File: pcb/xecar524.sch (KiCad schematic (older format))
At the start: 32 parts, among them J1 JTAG, J3 Conn_02x02_Odd_Even, U1 MCP1703A-3302_SOT89, U2 Atari_XE_Cartridge_Connector, U3 XC95144XL-TQ100, U4 SST39VF040

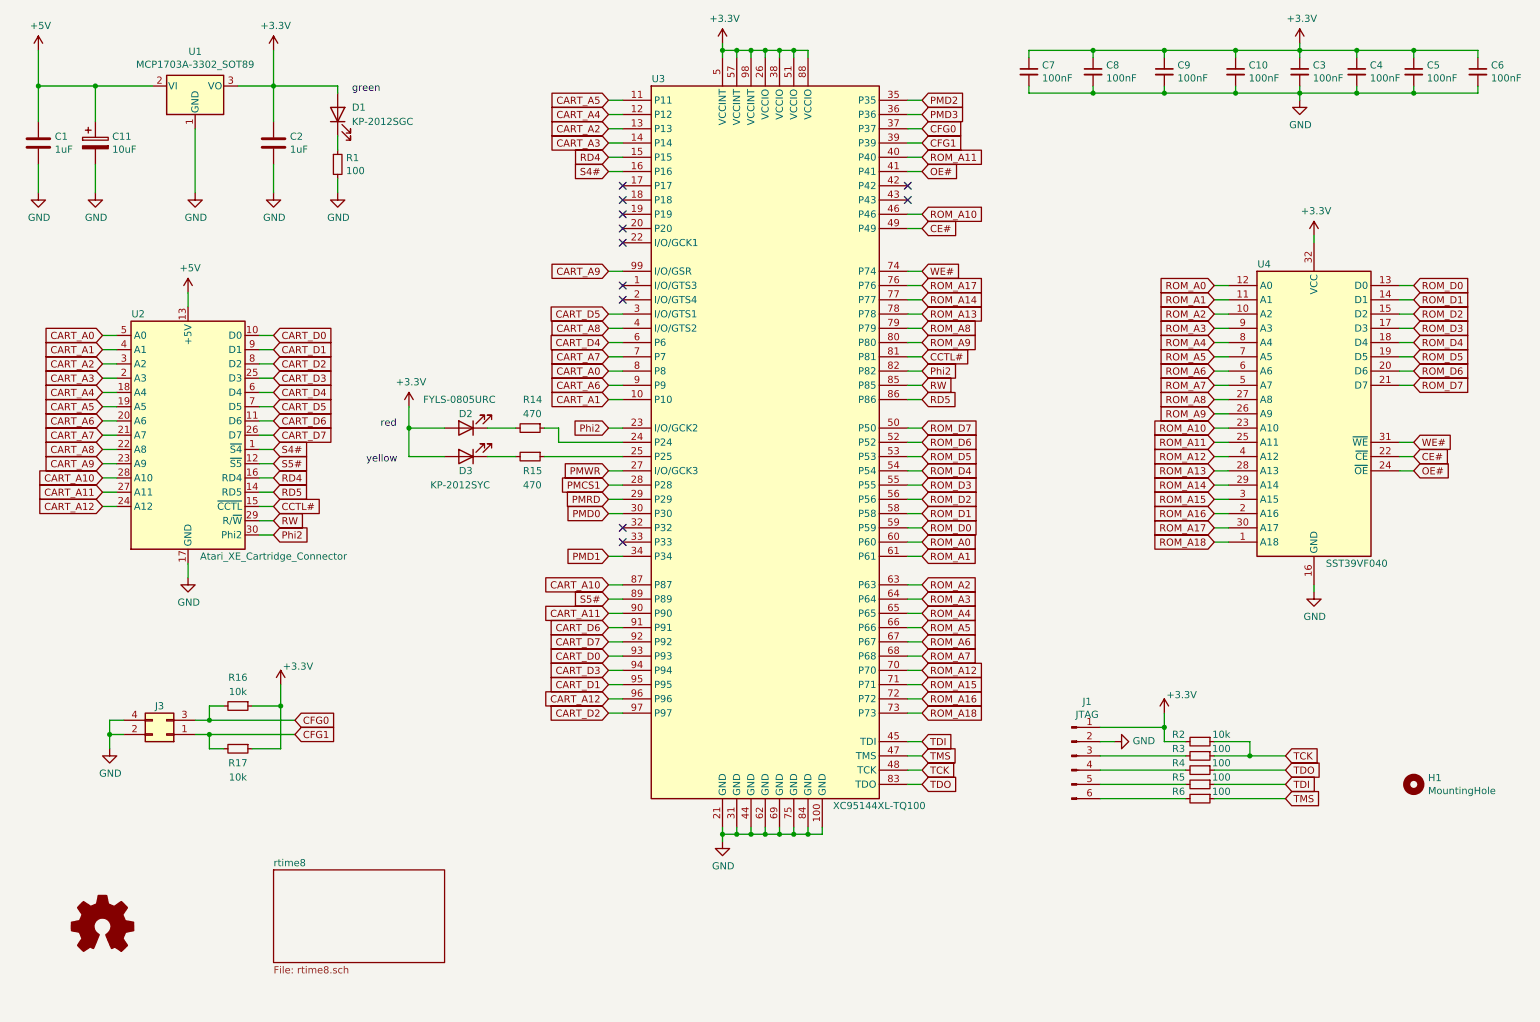
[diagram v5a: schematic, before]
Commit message: PCB, PLD: Add one configuration jumper
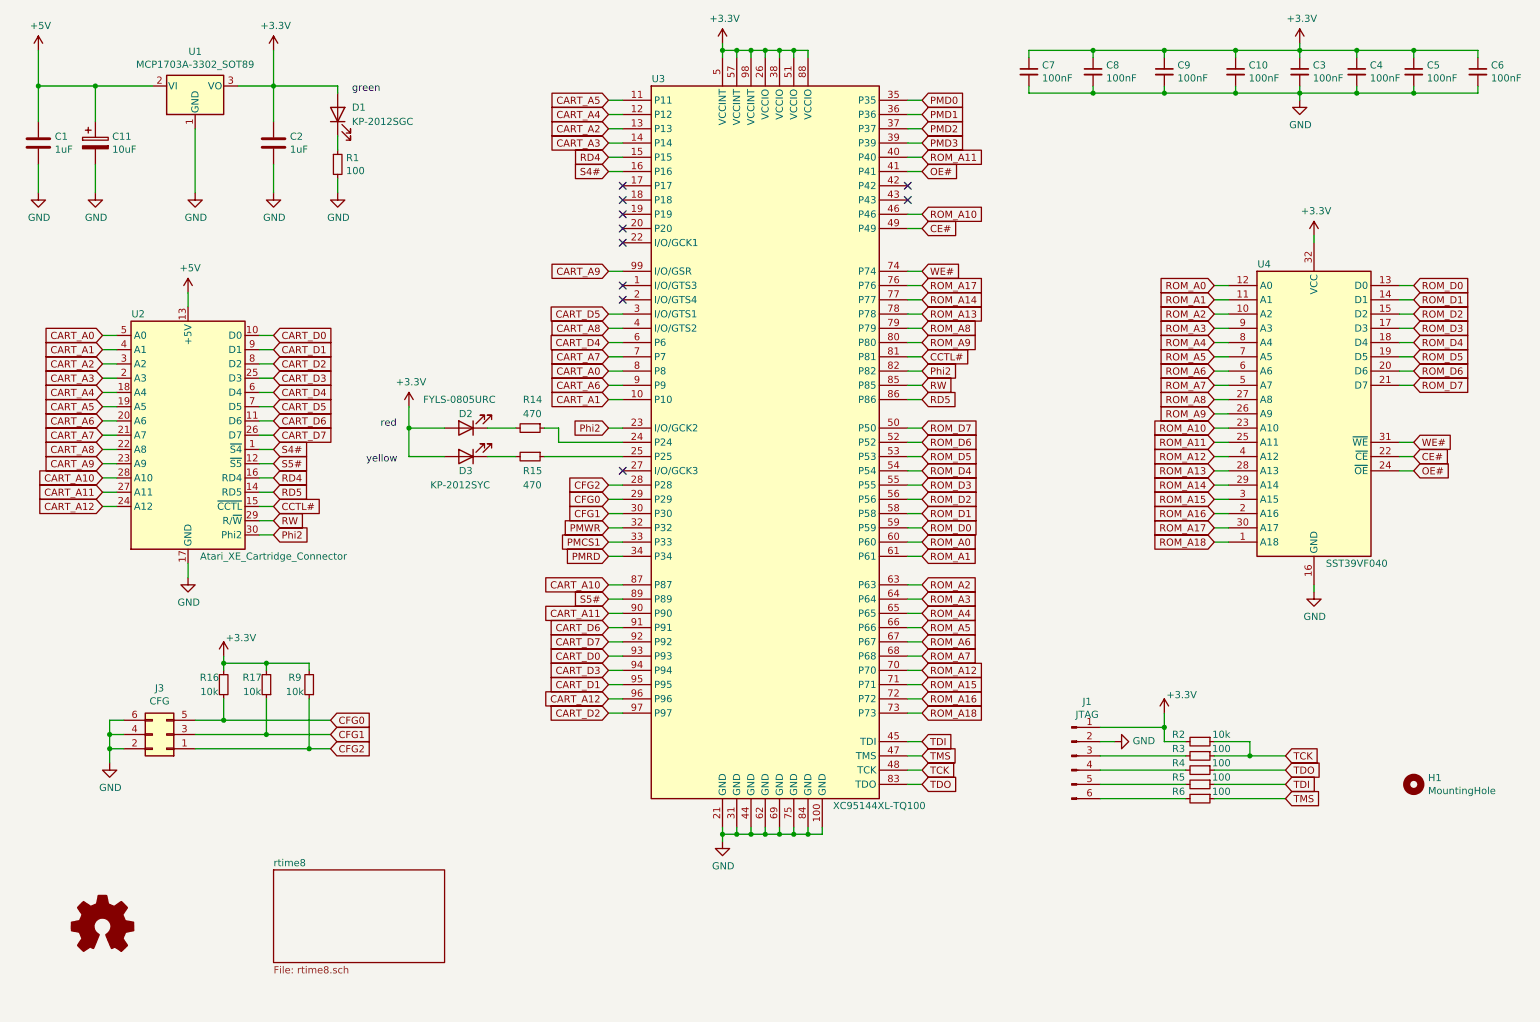
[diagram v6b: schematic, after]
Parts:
- removed J3: Conn_02x02_Odd_Even, Connector_PinHeader_2.54mm:PinHeader_2x02_P2.54mm_Horizontal, symbol Connector_Generic:Conn_02x02_Odd_Even
- added J3: CFG, Connector_PinHeader_2.54mm:PinHeader_2x03_P2.54mm_Horizontal, symbol Connector_Generic:Conn_02x03_Odd_Even
- added R9: 10k, Resistor_SMD:R_0805_2012Metric_Pad1.20x1.40mm_HandSolder, symbol Device:R_Small
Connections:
- net +3V3: now also R17.2, R9.2; no longer R17.1
- net CFG0: now also U3.29 (P29), J3.5 (Pin_5); no longer U3.37 (P37)
- net CFG1: now also R17.1, U3.30 (P30), J3.3 (Pin_3); no longer R17.2, U3.39 (P39)
- net GND: now also J3.2 (Pin_2), J3.4 (Pin_4), J3.6 (Pin_6)
- net PMCS1: now also U3.33 (P33); no longer U3.28 (P28)
- net PMD0: now also U3.35 (P35); no longer U3.30 (P30)
- net PMD1: now also U3.36 (P36); no longer U3.34 (P34)
- net PMD2: now also U3.37 (P37); no longer U3.35 (P35)
- net PMD3: now also U3.39 (P39); no longer U3.36 (P36)
- net PMRD: now also U3.34 (P34); no longer U3.29 (P29)
- net PMWR: now also U3.32 (P32); no longer U3.27 (I/O/GCK3)
- new net CFG2: J3.1 (Pin_1), R9.1, U3.28 (P28)
- no-connect marks 11 -> 10
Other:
- moved on the sheet: R16, R17
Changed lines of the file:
@@
 Text GLabel 6900 4050 2    50   Input ~ 0
 ROM_D2
-Text GLabel 4700 3950 0    50   Input ~ 0
+Text GLabel 4700 4350 0    50   Input ~ 0
 PMCS1
-Text GLabel 4700 4050 0    50   Input ~ 0
+Text GLabel 4700 4450 0    50   Input ~ 0
 PMRD
-Text GLabel 6900 1250 2    50   Input ~ 0
+Text GLabel 6900 1450 2    50   Input ~ 0
 PMD2
-Text GLabel 4700 4450 0    50   Input ~ 0
+Text GLabel 6900 1350 2    50   Input ~ 0
 PMD1
 Wire Wire Line
@@
 	4700 3950 4800 3950
 Wire Wire Line
-	4800 3850 4700 3850
+	4800 4250 4700 4250
 $Comp
 L Device:C_Polarized C11
@@
 Wire Wire Line
 	6900 1650 6800 1650
-Text GLabel 6900 1350 2    50   Input ~ 0
+Text GLabel 6900 1550 2    50   Input ~ 0
 PMD3
-Text GLabel 4700 4150 0    50   Input ~ 0
+Text GLabel 6900 1250 2    50   Input ~ 0
 PMD0
 Wire Wire Line
@@
 Wire Wire Line
 	4700 3550 4800 3550
-NoConn ~ 4800 4250
-NoConn ~ 4800 4350
+NoConn ~ 4800 3850
 NoConn ~ 4800 2650
 NoConn ~ 6800 1950
@@
 L Device:R_Small R16
 U 1 1 61313112
-P 2100 5500
-F 0 "R16" V 1900 5500 50  0000 C CNN
-F 1 "10k" V 2000 5500 50  0000 C CNN
-F 2 "Resistor_SMD:R_0805_2012Metric_Pad1.20x1.40mm_HandSolder" H 2100 5500 50  0001 C CNN
-F 3 "~" H 2100 5500 50  0001 C CNN
-	1    2100 5500
-	0    1    1    0
+P 2000 5350
+F 0 "R16" H 1900 5400 50  0000 C CNN
+F 1 "10k" H 1900 5300 50  0000 C CNN
+F 2 "Resistor_SMD:R_0805_2012Metric_Pad1.20x1.40mm_HandSolder" H 2000 5350 50  0001 C CNN
+F 3 "~" H 2000 5350 50  0001 C CNN
+	1    2000 5350
+	1    0    0    -1
 $EndComp
 $Comp
 L Device:R_Small R17
 U 1 1 61314B45
-P 2100 5800
-F 0 "R17" V 2200 5800 50  0000 C CNN
-F 1 "10k" V 2300 5800 50  0000 C CNN
-F 2 "Resistor_SMD:R_0805_2012Metric_Pad1.20x1.40mm_HandSolder" H 2100 5800 50  0001 C CNN
-F 3 "~" H 2100 5800 50  0001 C CNN
-	1    2100 5800
-	0    1    1    0
+P 2300 5350
+F 0 "R17" H 2400 5300 50  0000 C CNN
+F 1 "10k" H 2400 5400 50  0000 C CNN
+F 2 "Resistor_SMD:R_0805_2012Metric_Pad1.20x1.40mm_HandSolder" H 2300 5350 50  0001 C CNN
+F 3 "~" H 2300 5350 50  0001 C CNN
+	1    2300 5350
+	-1   0    0    1
 $EndComp
 $Comp
 L power:+3.3V #PWR05
 U 1 1 61314FD0
-P 2400 5350
-F 0 "#PWR05" H 2400 5200 50  0001 C CNN
-F 1 "+3.3V" H 2415 5478 50  0000 L CNN
-F 2 "" H 2400 5350 50  0001 C CNN
-F 3 "" H 2400 5350 50  0001 C CNN
-	1    2400 5350
+P 2000 5150
+F 0 "#PWR05" H 2000 5000 50  0001 C CNN
+F 1 "+3.3V" H 2015 5278 50  0000 L CNN
+F 2 "" H 2000 5150 50  0001 C CNN
+F 3 "" H 2000 5150 50  0001 C CNN
+	1    2000 5150
 	1    0    0    -1
 $EndComp
@@
 L power:GND #PWR04
 U 1 1 6132FDE7
-P 1200 5800
-F 0 "#PWR04" H 1200 5550 50  0001 C CNN
-F 1 "GND" H 1205 5627 50  0000 C CNN
-F 2 "" H 1200 5800 50  0001 C CNN
-F 3 "" H 1200 5800 50  0001 C CNN
-	1    1200 5800
-	1    0    0    -1
-$EndComp
-Wire Wire Line
-	1200 5800 1200 5700
+P 1200 5900
+F 0 "#PWR04" H 1200 5650 50  0001 C CNN
+F 1 "GND" H 1205 5727 50  0000 C CNN
+F 2 "" H 1200 5900 50  0001 C CNN
+F 3 "" H 1200 5900 50  0001 C CNN
+	1    1200 5900
+	1    0    0    -1
+$EndComp
+Wire Wire Line
+	1200 5900 1200 5800
 Wire Wire Line
 	1200 5700 1300 5700
@@
 	1200 5600 1300 5600
 Connection ~ 1200 5700
-Text GLabel 2500 5600 2    50   Input ~ 0
+Text GLabel 2750 5600 2    50   Input ~ 0
 CFG0
-Text GLabel 2500 5700 2    50   Input ~ 0
+Text GLabel 2750 5700 2    50   Input ~ 0
 CFG1
 Wire Wire Line
-	1800 5600 1900 5600
-Wire Wire Line
-	2500 5700 1900 5700
-Wire Wire Line
-	1900 5600 1900 5500
-Wire Wire Line
-	1900 5500 2000 5500
-Connection ~ 1900 5600
-Wire Wire Line
-	1900 5600 2500 5600
-Wire Wire Line
-	2200 5500 2400 5500
-Wire Wire Line
-	2400 5500 2400 5350
-Wire Wire Line
-	1900 5700 1900 5800
-Wire Wire Line
-	1900 5800 2000 5800
-Connection ~ 1900 5700
-Wire Wire Line
-	1900 5700 1800 5700
-Wire Wire Line
-	2200 5800 2400 5800
-Wire Wire Line
-	2400 5800 2400 5500
-Connection ~ 2400 5500
-Text GLabel 6900 1450 2    50   Input ~ 0
+	2000 5250 2000 5200
+Text GLabel 4700 4050 0    50   Input ~ 0
 CFG0
 Wire Wire Line
 	6900 1450 6800 1450
-Text GLabel 6900 1550 2    50   Input ~ 0
+Text GLabel 4700 4150 0    50   Input ~ 0
 CFG1
 Wire Wire Line
@@
 Wire Wire Line
 	3300 3750 3550 3750
-$Comp
-L Connector_Generic:Conn_02x02_Odd_Even J3
-U 1 1 61481D01
-P 1600 5700
-F 0 "J3" H 1650 5500 50  0000 C CNN
-F 1 "Conn_02x02_Odd_Even" H 1650 5826 50  0001 C CNN
-F 2 "Connector_PinHeader_2.54mm:PinHeader_2x02_P2.54mm_Horizontal" H 1600 5700 50  0001 C CNN
-F 3 "~" H 1600 5700 50  0001 C CNN
-	1    1600 5700
-	-1   0    0    1
-$EndComp
 $Sheet
 S 2350 6650 1200 650
@@
 	1    0    0    -1
 $EndComp
-Text GLabel 4700 3850 0    50   Input ~ 0
+Text GLabel 4700 4250 0    50   Input ~ 0
 PMWR
 Wire Wire Line
@@
 	1    0    0    -1
 $EndComp
+$Comp
+L Connector_Generic:Conn_02x03_Odd_Even J3
+U 1 1 60F81FA1
+P 1600 5700
+F 0 "J3" H 1650 5375 50  0000 C CNN
+F 1 "CFG" H 1650 5466 50  0000 C CNN
+F 2 "Connector_PinHeader_2.54mm:PinHeader_2x03_P2.54mm_Horizontal" H 1600 5700 50  0001 C CNN
+F 3 "~" H 1600 5700 50  0001 C CNN
+	1    1600 5700
+	-1   0    0    1
+$EndComp
+Wire Wire Line
+	1800 5700 2300 5700
+Wire Wire Line
+	1800 5600 2000 5600
+Wire Wire Line
+	2000 5200 2300 5200
+Wire Wire Line
+	2300 5200 2300 5250
+Connection ~ 2000 5200
+Wire Wire Line
+	2000 5200 2000 5150
+$Comp
+L Device:R_Small R9
+U 1 1 60FC2B6D
+P 2600 5350
+F 0 "R9" H 2700 5300 50  0000 C CNN
+F 1 "10k" H 2700 5400 50  0000 C CNN
+F 2 "Resistor_SMD:R_0805_2012Metric_Pad1.20x1.40mm_HandSolder" H 2600 5350 50  0001 C CNN
+F 3 "~" H 2600 5350 50  0001 C CNN
+	1    2600 5350
+	-1   0    0    1
+$EndComp
+Text GLabel 2750 5800 2    50   Input ~ 0
+CFG2
+Wire Wire Line
+	2750 5800 2600 5800
+Wire Wire Line
+	1200 5800 1300 5800
+Connection ~ 1200 5800
+Wire Wire Line
+	1200 5800 1200 5700
+Wire Wire Line
+	2000 5450 2000 5600
+Connection ~ 2000 5600
+Wire Wire Line
+	2000 5600 2750 5600
+Wire Wire Line
+	2300 5450 2300 5700
+Connection ~ 2300 5700
+Wire Wire Line
+	2300 5700 2750 5700
+Wire Wire Line
+	2600 5450 2600 5800
+Connection ~ 2600 5800
+Wire Wire Line
+	2600 5800 1800 5800
+Wire Wire Line
+	2300 5200 2600 5200
+Wire Wire Line
+	2600 5200 2600 5250
+Connection ~ 2300 5200
+Wire Wire Line
+	4700 4350 4800 4350
+Text GLabel 4700 3950 0    50   Input ~ 0
+CFG2
 $EndSCHEMATC

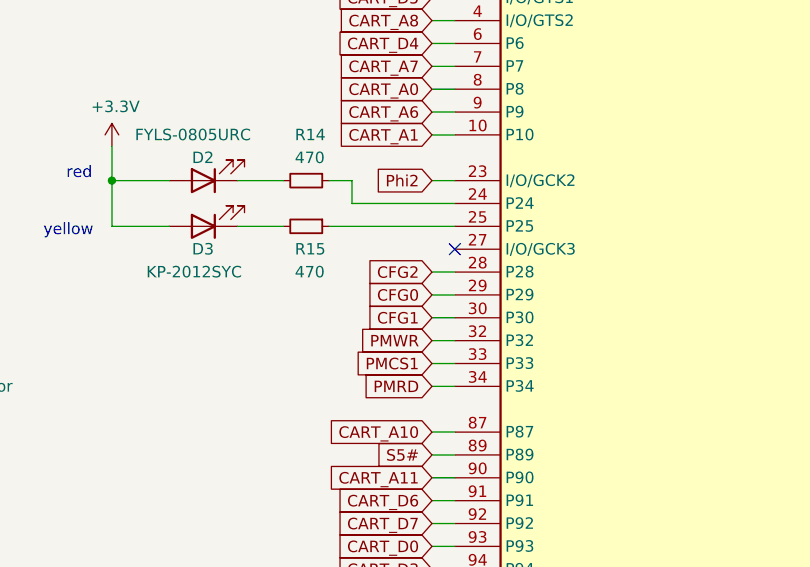
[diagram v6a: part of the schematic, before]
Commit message: PCB, PLD: Add a connection between PLD and microcontroller
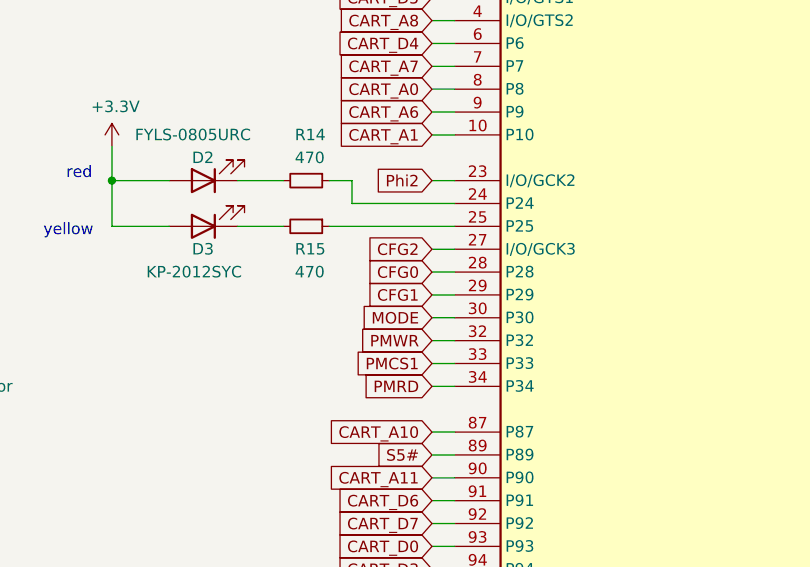
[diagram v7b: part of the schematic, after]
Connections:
- net CFG0: now also U3.28 (P28); no longer U3.29 (P29)
- net CFG1: now also U3.29 (P29); no longer U3.30 (P30)
- net CFG2: now also U3.27 (I/O/GCK3); no longer U3.28 (P28)
- new net MODE: U3.30 (P30)
- no-connect marks 10 -> 9
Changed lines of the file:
@@
 PMD1
 Wire Wire Line
-	4700 4150 4800 4150
-Wire Wire Line
-	4800 4050 4700 4050
-Wire Wire Line
-	4700 3950 4800 3950
+	4700 4050 4800 4050
+Wire Wire Line
+	4800 3950 4700 3950
+Wire Wire Line
+	4700 3850 4800 3850
 Wire Wire Line
 	4800 4250 4700 4250
@@
 Wire Wire Line
 	4700 3550 4800 3550
-NoConn ~ 4800 3850
 NoConn ~ 4800 2650
 NoConn ~ 6800 1950
@@
 Wire Wire Line
 	2000 5250 2000 5200
+Text GLabel 4700 3950 0    50   Input ~ 0
+CFG0
+Wire Wire Line
+	6900 1450 6800 1450
 Text GLabel 4700 4050 0    50   Input ~ 0
-CFG0
-Wire Wire Line
-	6900 1450 6800 1450
-Text GLabel 4700 4150 0    50   Input ~ 0
 CFG1
 Wire Wire Line
@@
 Wire Wire Line
 	4700 4350 4800 4350
-Text GLabel 4700 3950 0    50   Input ~ 0
+Text GLabel 4700 3850 0    50   Input ~ 0
 CFG2
+Text GLabel 4700 4150 0    50   Input ~ 0
+MODE
+Wire Wire Line
+	4700 4150 4800 4150
 $EndSCHEMATC

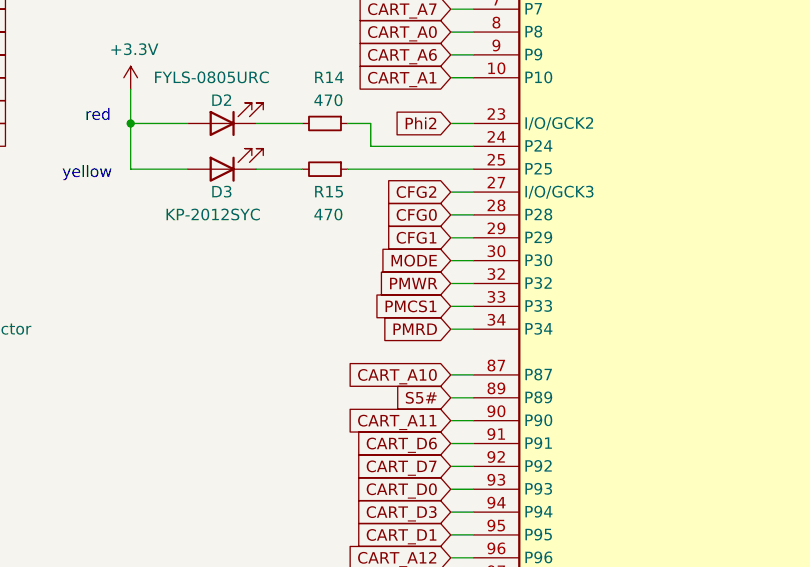
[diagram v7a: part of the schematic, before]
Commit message: Tweak connections between PLD and uC
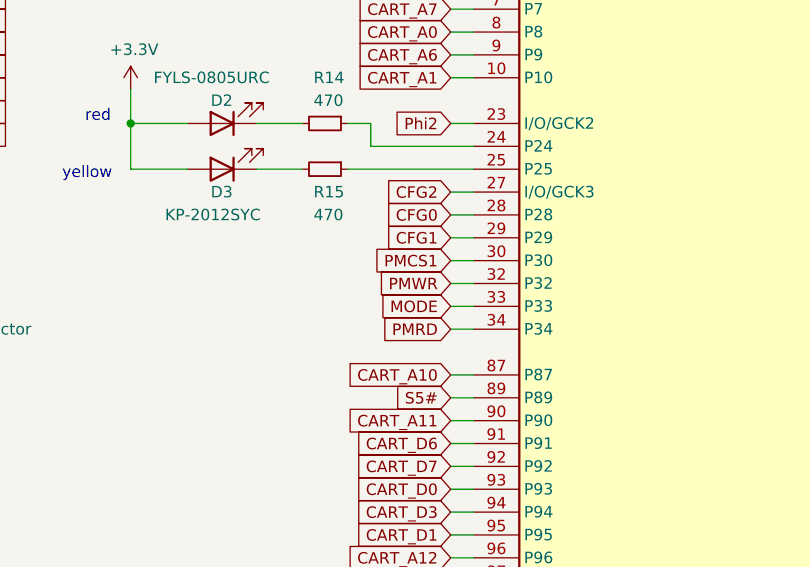
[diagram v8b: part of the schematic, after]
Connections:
- net MODE: now also U3.33 (P33); no longer U3.30 (P30)
- net PMCS1: now also U3.30 (P30); no longer U3.33 (P33)
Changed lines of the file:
@@
 Text GLabel 6900 4050 2    50   Input ~ 0
 ROM_D2
-Text GLabel 4700 4350 0    50   Input ~ 0
+Text GLabel 4700 4150 0    50   Input ~ 0
 PMCS1
 Text GLabel 4700 4450 0    50   Input ~ 0
@@
 Text GLabel 4700 3850 0    50   Input ~ 0
 CFG2
-Text GLabel 4700 4150 0    50   Input ~ 0
+Text GLabel 4700 4350 0    50   Input ~ 0
 MODE
 Wire Wire Line
